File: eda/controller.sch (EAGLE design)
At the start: 94 parts, among them U1 STM32F405/7R, U10 3.3V, U2 ISL83491SOIC, U3 ISL83491SOIC, U4 ISL83491SOIC, U5 ISL83491SOIC, U6 LM3525, U7 BLE-HM-10, U8 XBEE-1NOSILK, U9 TPS54227DDA, X1 MICROSD-SOCKETAMPHENOL, Y1 8 MHz/C_L=18 pF

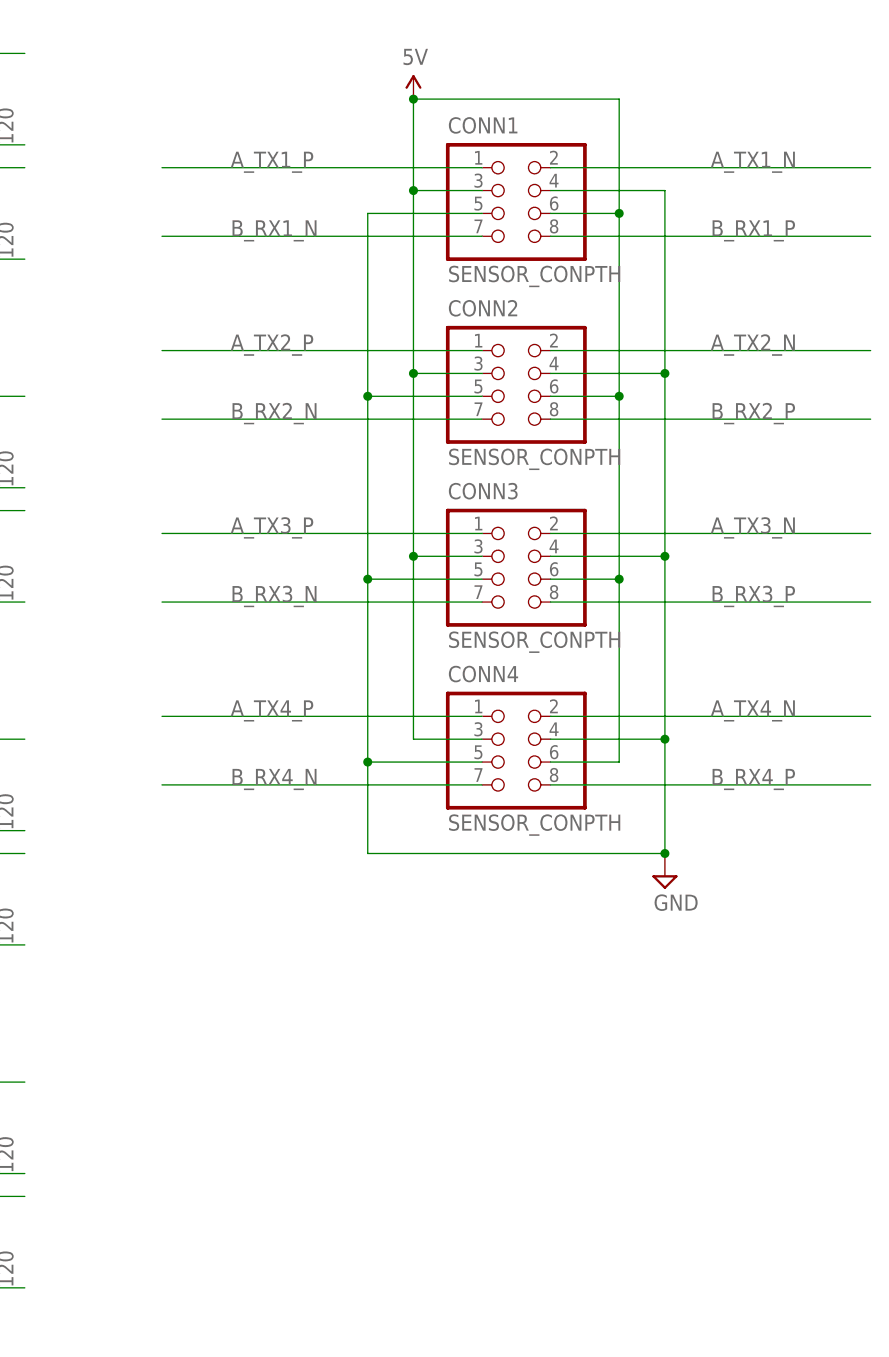
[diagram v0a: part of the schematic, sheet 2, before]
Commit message: Change smartsensor connectors to 2x5 on controller board
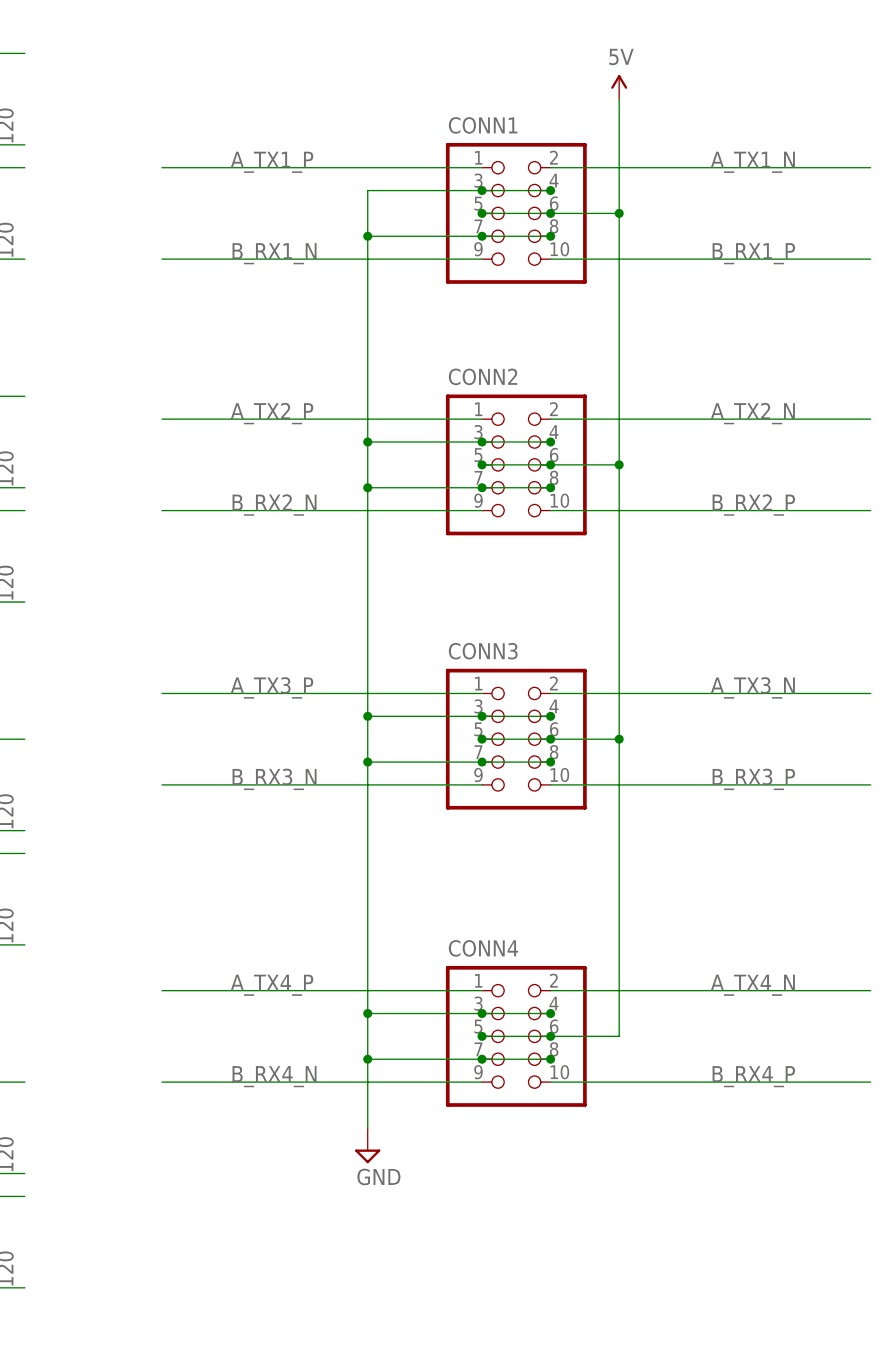
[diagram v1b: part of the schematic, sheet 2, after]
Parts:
- CONN1, CONN2, CONN3, CONN4: value SENSOR_CONPTH -> (none); device pie:SENSOR_CONPTH -> pie:SENSOR_CON_5PINPTH
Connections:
- net 5V: now also CONN1.5, CONN2.5, CONN3.5, CONN4.5; no longer CONN1.3, CONN2.3, CONN3.3, CONN4.3
- net B_RX1_N: now also CONN1.9; no longer CONN1.7
- net B_RX1_P: now also CONN1.10; no longer CONN1.8
- net B_RX2_N: now also CONN2.9; no longer CONN2.7
- net B_RX2_P: now also CONN2.10; no longer CONN2.8
- net B_RX3_N: now also CONN3.9; no longer CONN3.7
- net B_RX3_P: now also CONN3.10; no longer CONN3.8
- net B_RX4_N: now also CONN4.9; no longer CONN4.7
- net B_RX4_P: now also CONN4.10; no longer CONN4.8
- net GND: now also CONN1.3, CONN1.7, CONN1.8, CONN2.3, CONN2.7, CONN2.8, CONN3.3, CONN3.7, CONN3.8, CONN4.3, CONN4.7, CONN4.8; no longer CONN1.5, CONN2.5, CONN3.5, CONN4.5

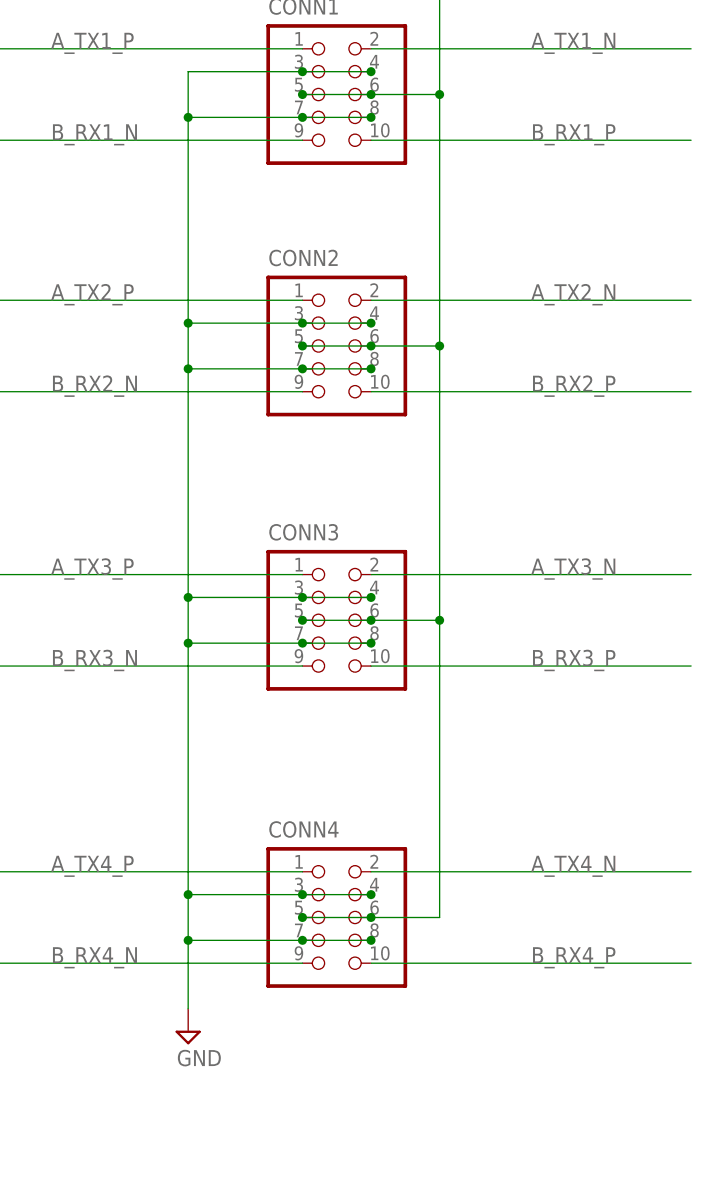
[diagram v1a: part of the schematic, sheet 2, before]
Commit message: Minor routing fixes on grizzly and controller.
Edit rqou: Hopefully fixed fun merge problems between this commit
and Andrew Wang's.
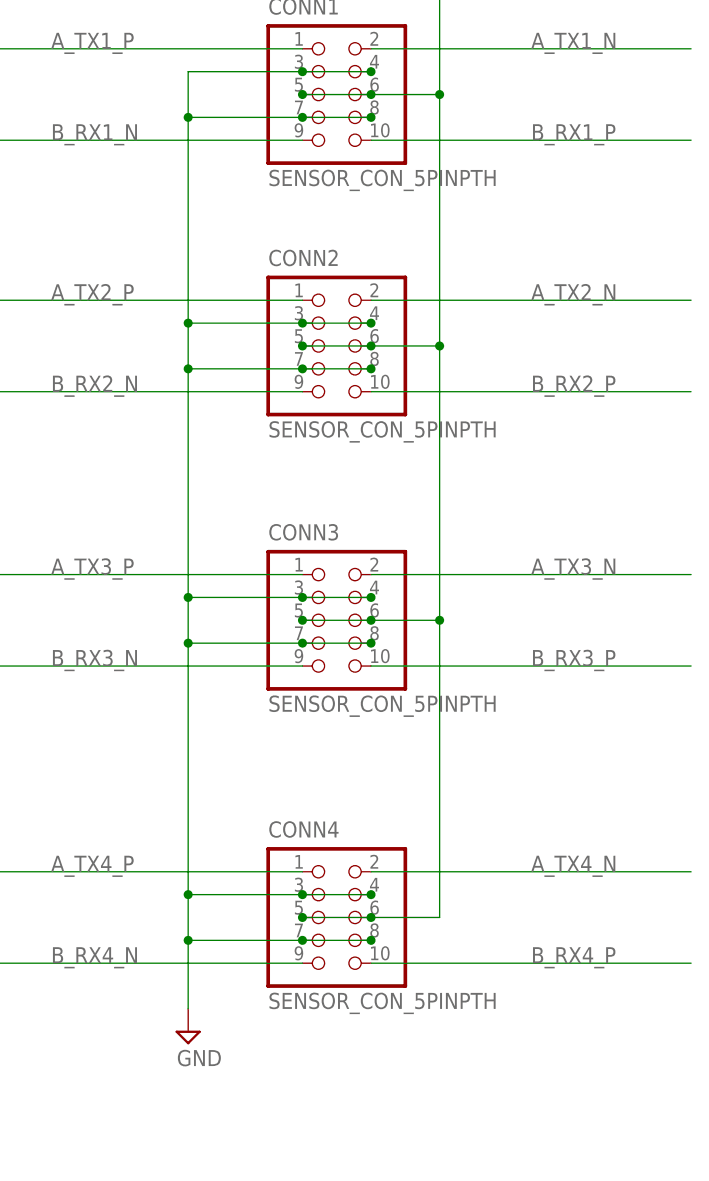
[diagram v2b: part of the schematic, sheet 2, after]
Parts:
- CONN1, CONN2, CONN3, CONN4: value (none) -> SENSOR_CON_5PINPTH
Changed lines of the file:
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@@
 <part name="U$12" library="pie" deviceset="5V" device=""/>
 <part name="SUPPLY20" library="pie" deviceset="GND" device=""/>
-<part name="CONN1" library="pie" deviceset="SENSOR_CON_5PIN" device="PTH"/>
-<part name="CONN2" library="pie" deviceset="SENSOR_CON_5PIN" device="PTH"/>
-<part name="CONN3" library="pie" deviceset="SENSOR_CON_5PIN" device="PTH"/>
-<part name="CONN4" library="pie" deviceset="SENSOR_CON_5PIN" device="PTH"/>
+<part name="CONN1" library="pie" deviceset="SENSOR_CON_5PIN" device="PTH" value="SENSOR_CON_5PINPTH"/>
+<part name="CONN2" library="pie" deviceset="SENSOR_CON_5PIN" device="PTH" value="SENSOR_CON_5PINPTH"/>
+<part name="CONN3" library="pie" deviceset="SENSOR_CON_5PIN" device="PTH" value="SENSOR_CON_5PINPTH"/>
+<part name="CONN4" library="pie" deviceset="SENSOR_CON_5PIN" device="PTH" value="SENSOR_CON_5PINPTH"/>
 <part name="U$17" library="pie" deviceset="5V" device=""/>
 <part name="SUPPLY21" library="pie" deviceset="GND" device=""/>
